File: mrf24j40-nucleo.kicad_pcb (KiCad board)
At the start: 2 copper layers, 28.6 x 25.4 mm, 2 parts, among them M1 MRF24J40MA_TRANSEIVER_MODULE, P1 CONN_02X08

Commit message: Add version number
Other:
- board text added: "v1"
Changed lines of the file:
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@@
     (links 11)
     (no_connects 0)
-    (area 83.109999 15.693142 214.320002 85.415002)
+    (area 69.620001 15.693142 214.320002 85.415002)
     (thickness 1.6)
-    (drawings 15)
+    (drawings 16)
     (tracks 55)
     (zones 0)
@@
     )
   )
+  (gr_text v1 (at 100.33 33.655) (layer F.SilkS)
+    (effects (font (size 1 1) (thickness 0.25)))
+  )
   (gr_text "Nucleo Keppeltje\n" (at 90.805 33.655) (layer F.SilkS)

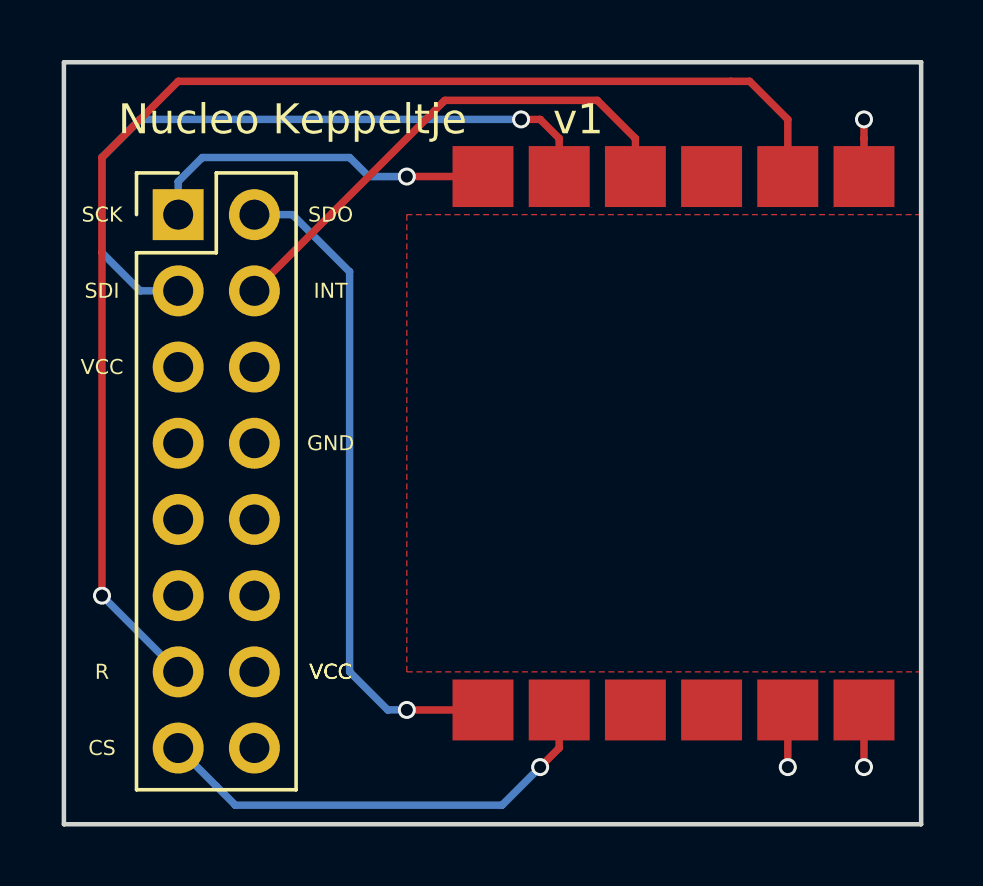
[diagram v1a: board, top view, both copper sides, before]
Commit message: Fix in 3.3V pin/Minor reroute
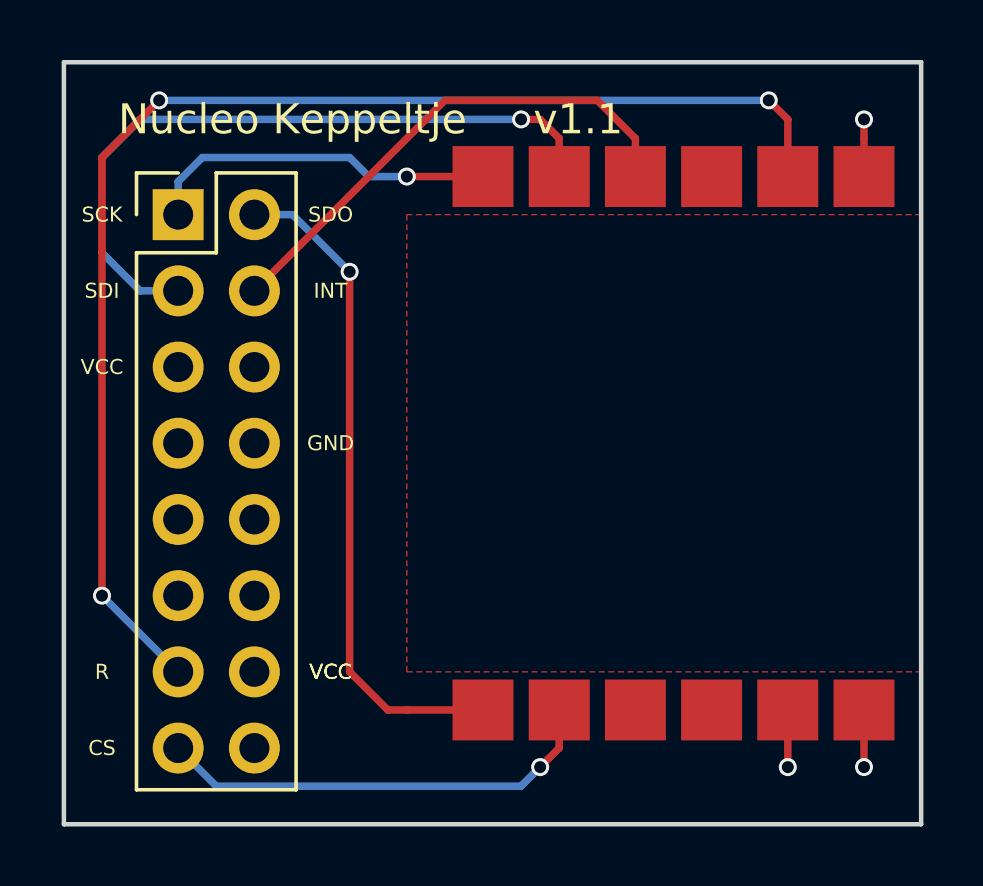
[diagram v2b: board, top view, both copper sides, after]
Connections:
- P1 pad 14: +3V3 -> Net-(P1-Pad14)
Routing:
- net RESET: track 44.5 -> 44.0 mm, vias 1 -> 3
- net CS: track 15.5 -> 15.0 mm
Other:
- board text added: "v1.1"
- board text removed: "v1"
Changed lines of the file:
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@@
 (kicad_pcb (version 4) (host pcbnew 4.0.5)
   (general
-    (links 11)
+    (links 10)
     (no_connects 0)
-    (area 69.620001 15.693142 214.320002 85.415002)
+    (area 83.109999 15.693142 214.320002 85.415002)
     (thickness 1.6)
     (drawings 16)
-    (tracks 55)
+    (tracks 54)
     (zones 0)
     (modules 2)
-    (nets 17)
+    (nets 18)
   )
   (page User 200 119.99)
@@
     (pad_to_mask_clearance 0.2)
     (aux_axis_origin 185.42 108.585)
-    (grid_origin 83.185 57.15)
+    (grid_origin 83.185 57.785)
     (visible_elements FFFFF77F)
     (pcbplotparams
@@
   (net 15 "Net-(P1-Pad12)")
   (net 16 "Net-(P1-Pad16)")
+  (net 17 "Net-(P1-Pad14)")
   (net_class Default "This is the default net class."
     (clearance 0.2)
@@
     (add_net "Net-(P1-Pad11)")
     (add_net "Net-(P1-Pad12)")
+    (add_net "Net-(P1-Pad14)")
     (add_net "Net-(P1-Pad16)")
     (add_net "Net-(P1-Pad6)")
@@
       (net 2 RESET))
     (pad 14 thru_hole oval (at 2.54 15.24) (size 1.7 1.7) (drill 1) (layers *.Cu *.Mask)
-      (net 9 +3V3))
+      (net 17 "Net-(P1-Pad14)"))
     (pad 15 thru_hole oval (at 0 17.78) (size 1.7 1.7) (drill 1) (layers *.Cu *.Mask)
       (net 8 CS))
@@
     )
   )
-  (gr_text v1 (at 100.33 33.655) (layer F.SilkS)
+  (gr_text "Nucleo Keppeltje\n" (at 90.805 33.655) (layer F.SilkS)
     (effects (font (size 1 1) (thickness 0.25)))
   )
-  (gr_text "Nucleo Keppeltje\n" (at 90.805 33.655) (layer F.SilkS)
+  (gr_text v1.1 (at 100.33 33.655) (layer F.SilkS)
     (effects (font (size 1 1) (thickness 0.25)))
   )
@@
   (via (at 107.315 55.245) (size 0.6) (drill 0.4) (layers F.Cu B.Cu) (net 1))
   (segment (start 107.315 53.34) (end 107.315 55.245) (width 0.25) (layer F.Cu) (net 1))
+  (segment (start 86.36 33.02) (end 84.455 34.925) (width 0.25) (layer F.Cu) (net 2))
+  (via (at 86.36 33.02) (size 0.6) (drill 0.4) (layers F.Cu B.Cu) (net 2))
+  (segment (start 106.68 33.02) (end 86.36 33.02) (width 0.25) (layer B.Cu) (net 2))
+  (via (at 106.68 33.02) (size 0.6) (drill 0.4) (layers F.Cu B.Cu) (net 2))
+  (segment (start 107.315 33.655) (end 106.68 33.02) (width 0.25) (layer F.Cu) (net 2))
   (segment (start 84.455 34.925) (end 84.455 49.53) (width 0.25) (layer F.Cu) (net 2))
   (segment (start 84.455 49.53) (end 86.995 52.07) (width 0.25) (layer B.Cu) (net 2))
   (via (at 84.455 49.53) (size 0.6) (drill 0.4) (layers F.Cu B.Cu) (net 2))
-  (segment (start 105.41 32.385) (end 86.995 32.385) (width 0.25) (layer F.Cu) (net 2))
-  (segment (start 106.045 32.385) (end 105.41 32.385) (width 0.25) (layer F.Cu) (net 2))
   (segment (start 107.315 35.56) (end 107.315 33.655) (width 0.25) (layer F.Cu) (net 2))
-  (segment (start 107.315 33.655) (end 106.045 32.385) (width 0.25) (layer F.Cu) (net 2))
-  (segment (start 86.995 32.385) (end 84.455 34.925) (width 0.25) (layer F.Cu) (net 2))
+  (segment (start 95.885 33.02) (end 100.965 33.02) (width 0.25) (layer F.Cu) (net 4))
+  (segment (start 89.535 39.37) (end 95.804646 33.100354) (width 0.25) (layer F.Cu) (net 4))
   (segment (start 102.235 34.29) (end 102.235 35.56) (width 0.25) (layer F.Cu) (net 4))
   (segment (start 100.965 33.02) (end 102.235 34.29) (width 0.25) (layer F.Cu) (net 4))
-  (segment (start 95.885 33.02) (end 100.965 33.02) (width 0.25) (layer F.Cu) (net 4))
-  (segment (start 95.804646 33.100354) (end 95.885 33.02) (width 0.25) (layer F.Cu) (net 4))
-  (segment (start 89.535 39.37) (end 95.804646 33.100354) (width 0.25) (layer F.Cu) (net 4))
+  (segment (start 98.425 33.655) (end 85.725 33.655) (width 0.25) (layer B.Cu) (net 5))
+  (via (at 98.425 33.655) (size 0.6) (drill 0.4) (layers F.Cu B.Cu) (net 5))
   (segment (start 99.695 34.29) (end 99.695 35.56) (width 0.25) (layer F.Cu) (net 5))
   (segment (start 99.06 33.655) (end 99.695 34.29) (width 0.25) (layer F.Cu) (net 5))
   (segment (start 98.425 33.655) (end 99.06 33.655) (width 0.25) (layer F.Cu) (net 5))
-  (via (at 98.425 33.655) (size 0.6) (drill 0.4) (layers F.Cu B.Cu) (net 5))
-  (segment (start 98.425 33.655) (end 85.725 33.655) (width 0.25) (layer B.Cu) (net 5))
   (segment (start 85.725 33.655) (end 84.455 34.925) (width 0.25) (layer B.Cu) (net 5))
   (segment (start 84.455 34.925) (end 84.455 38.1) (width 0.25) (layer B.Cu) (net 5))
@@
   (via (at 94.615 35.56) (size 0.6) (drill 0.4) (layers F.Cu B.Cu) (net 6))
   (segment (start 97.155 35.56) (end 94.615 35.56) (width 0.25) (layer F.Cu) (net 6))
+  (via (at 92.71 38.735) (size 0.6) (drill 0.4) (layers F.Cu B.Cu) (net 7))
+  (segment (start 92.71 38.735) (end 92.71 52.07) (width 0.25) (layer F.Cu) (net 7))
+  (segment (start 93.98 53.34) (end 92.71 52.07) (width 0.25) (layer F.Cu) (net 7))
+  (segment (start 94.615 53.34) (end 93.98 53.34) (width 0.25) (layer F.Cu) (net 7))
   (segment (start 94.615 53.34) (end 97.155 53.34) (width 0.25) (layer F.Cu) (net 7))
-  (segment (start 93.98 53.34) (end 94.615 53.34) (width 0.25) (layer B.Cu) (net 7))
-  (via (at 94.615 53.34) (size 0.6) (drill 0.4) (layers F.Cu B.Cu) (net 7))
-  (segment (start 92.71 52.07) (end 93.98 53.34) (width 0.25) (layer B.Cu) (net 7))
-  (segment (start 92.71 38.735) (end 92.71 52.07) (width 0.25) (layer B.Cu) (net 7))
   (segment (start 90.805 36.83) (end 92.71 38.735) (width 0.25) (layer B.Cu) (net 7))
   (segment (start 89.535 36.83) (end 90.805 36.83) (width 0.25) (layer B.Cu) (net 7))
-  (segment (start 97.79 56.515) (end 88.9 56.515) (width 0.25) (layer B.Cu) (net 8))
-  (segment (start 88.9 56.515) (end 88.265 55.88) (width 0.25) (layer B.Cu) (net 8))
+  (segment (start 98.425 55.88) (end 99.06 55.245) (width 0.25) (layer B.Cu) (net 8))
+  (segment (start 88.265 55.88) (end 98.425 55.88) (width 0.25) (layer B.Cu) (net 8))
   (segment (start 88.265 55.88) (end 86.995 54.61) (width 0.25) (layer B.Cu) (net 8))
-  (segment (start 99.06 55.245) (end 97.79 56.515) (width 0.25) (layer B.Cu) (net 8))
   (via (at 99.06 55.245) (size 0.6) (drill 0.4) (layers F.Cu B.Cu) (net 8))
   (segment (start 99.695 54.61) (end 99.06 55.245) (width 0.25) (layer F.Cu) (net 8))
